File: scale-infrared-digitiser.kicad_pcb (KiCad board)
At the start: 2 copper layers, 8 x 166 mm, 115 parts, among them IC0 LM324PT, IC1 LM324PT, IC2 LM324PT, IC3 LM324PT, IC4 74HC4067PW,118, IC5 74HC4067PW,118, J0 Conn_02x04_TRNS, J1 Conn_02x04_RECV, Q1 T2N7002AK, Q10 T2N7002AK, Q11 T2N7002AK, Q12 T2N7002AK, Q13 T2N7002AK, Q14 T2N7002AK, Q15 T2N7002AK, Q16 T2N7002AK, Q2 T2N7002AK, Q3 T2N7002AK, Q4 T2N7002AK, Q5 T2N7002AK, Q6 T2N7002AK, Q7 T2N7002AK, Q8 T2N7002AK, Q9 T2N7002AK

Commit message: short sides almost complete
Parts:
- removed C13, C19, C25, C6: 1u, Capacitor_SMD:C_0603_1608Metric
- moved IC5 173.5 mm to (200.4, 96.5), turned to 90 degrees
- moved J1 173.4 mm to (206.9, 97.7), turned to 90 degrees
- moved LED0 140.6 mm to (70.1, 81.7), turned to 90 degrees
- moved D_photo15 139.0 mm to (190.9, 93.7), turned to 90 degrees
- moved LED1 138.3 mm to (78.2, 81.7), turned to 90 degrees
- moved Q1 136.9 mm to (69.7, 85.9), turned to 90 degrees
- moved LED2 136.0 mm to (86.2, 81.7), turned to 90 degrees
- moved LED3 133.7 mm to (94.3, 81.7), turned to 90 degrees
- moved D_photo14 129.0 mm to (182.9, 93.7), turned to 90 degrees
- moved Q2 128.3 mm to (81.4, 74.9), turned to 90 degrees
- moved R1 126.6 mm to (70.5, 70.6)
- moved D_photo11 125.5 mm to (158.7, 93.7), turned to 90 degrees
- moved Q3 125.1 mm to (86.0, 74.9), turned to 90 degrees
- moved Q4 122.2 mm to (90.7, 74.9), turned to 90 degrees
- moved D_photo13 119.5 mm to (174.8, 93.7), turned to 90 degrees
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- renumbered D_photo14 to D_photo10, D_photo15 to D_photo11, D_photo8 to D_photo12, D_photo9 to D_photo13, D_photo10 to D_photo14, D_photo11 to D_photo15, D_photo12 to D_photo8, D_photo13 to D_photo9
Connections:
- C21 pad 1: /PHT_DAT_8 -> /PHT_DAT_10
- C22 pad 2: /PHT_DAT_9 -> /PHT_DAT_11
- C23 pad 1: /PHT_DAT_10 -> /PHT_DAT_8
- C24 pad 2: /PHT_DAT_11 -> /PHT_DAT_9
- D_photo0 pad 1: /PHT_DAT_0 -> /PHT_DAT_1
- D_photo1 pad 1: /PHT_DAT_1 -> /PHT_DAT_0
- D_photo10 pad 1: /PHT_DAT_14 -> /PHT_DAT_15
- D_photo11 pad 1: /PHT_DAT_15 -> /PHT_DAT_14
- D_photo12 pad 1: /PHT_DAT_8 -> /PHT_DAT_11
- D_photo13 pad 1: /PHT_DAT_9 -> /PHT_DAT_10
- D_photo14 pad 1: /PHT_DAT_10 -> /PHT_DAT_9
- D_photo15 pad 1: /PHT_DAT_11 -> /PHT_DAT_8
- D_photo2 pad 1: /PHT_DAT_2 -> /PHT_DAT_3
- D_photo3 pad 1: /PHT_DAT_3 -> /PHT_DAT_2
- D_photo4 pad 1: /PHT_DAT_4 -> /PHT_DAT_5
- D_photo5 pad 1: /PHT_DAT_5 -> /PHT_DAT_4
- D_photo6 pad 1: /PHT_DAT_6 -> /PHT_DAT_7
- D_photo7 pad 1: /PHT_DAT_7 -> /PHT_DAT_6
- D_photo8 pad 1: /PHT_DAT_12 -> /PHT_DAT_13
- D_photo9 pad 1: /PHT_DAT_13 -> /PHT_DAT_12
- IC0 pad 4: /3V3 -> /3V3_RECV
- IC1 pad 4: /3V3 -> /3V3_RECV
- IC2 pad 4: /3V3 -> /3V3_RECV
- IC3 pad 13: /PHT_DAT_11 -> /PHT_DAT_9
- IC3 pad 2: /PHT_DAT_8 -> /PHT_DAT_10
- IC3 pad 4: /3V3 -> /3V3_RECV
- IC3 pad 6: /PHT_DAT_9 -> /PHT_DAT_11
- IC3 pad 9: /PHT_DAT_10 -> /PHT_DAT_8
- IC4 pad 12: GND -> GND1
- IC4 pad 15: GND -> GND1
- IC4 pad 24: /3V3 -> /3V3_TRNS
- IC5 pad 24: /3V3 -> /3V3_RECV
- J0 pad 5: /3V3 -> /3V3_TRNS
- J0 pad 7: GND -> GND1
- J0 pad 8: GND -> GND1
- J1 pad 1: /SEL_RECV_3 -> /MCU_RECV_DAT
- J1 pad 2: /SEL_RECV_2 -> /SEL_RECV_3
- J1 pad 3: /SEL_RECV_1 -> /SEL_RECV_0
- J1 pad 4: /SEL_RECV_0 -> /SEL_RECV_2
- J1 pad 5: /3V3 -> /SEL_RECV_1
- J1 pad 6: /MCU_RECV_DAT -> /3V3_RECV
- Q1 pad 2: GND -> GND1
- Q10 pad 2: GND -> GND1
- Q11 pad 2: GND -> GND1
- Q12 pad 2: GND -> GND1
- Q13 pad 2: GND -> GND1
- Q14 pad 2: GND -> GND1
- Q15 pad 2: GND -> GND1
- Q16 pad 2: GND -> GND1
- Q2 pad 2: GND -> GND1
- Q3 pad 2: GND -> GND1
- Q4 pad 2: GND -> GND1
- Q5 pad 2: GND -> GND1
- Q6 pad 2: GND -> GND1
- Q7 pad 2: GND -> GND1
- Q8 pad 2: GND -> GND1
- Q9 pad 2: GND -> GND1
- R1 pad 2: /3V3 -> /3V3_TRNS
- R10 pad 2: /3V3 -> /3V3_TRNS
- R11 pad 2: /3V3 -> /3V3_TRNS
- R12 pad 2: /3V3 -> /3V3_TRNS
- R13 pad 2: /3V3 -> /3V3_TRNS
- R14 pad 2: /3V3 -> /3V3_TRNS
- R15 pad 2: /3V3 -> /3V3_TRNS
- R16 pad 2: /3V3 -> /3V3_TRNS
- R18 pad 2: /3V3 -> /3V3_RECV
- R2 pad 2: /3V3 -> /3V3_TRNS
- R3 pad 2: /3V3 -> /3V3_TRNS
- R31 pad 2: /PHT_DAT_8 -> /PHT_DAT_10
- R32 pad 1: /PHT_DAT_9 -> /PHT_DAT_11
- R33 pad 2: /PHT_DAT_10 -> /PHT_DAT_8
- R34 pad 1: /PHT_DAT_11 -> /PHT_DAT_9
- R4 pad 2: /3V3 -> /3V3_TRNS
- R5 pad 2: /3V3 -> /3V3_TRNS
- R6 pad 2: /3V3 -> /3V3_TRNS
- R7 pad 2: /3V3 -> /3V3_TRNS
- R8 pad 2: /3V3 -> /3V3_TRNS
- R9 pad 2: /3V3 -> /3V3_TRNS
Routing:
- net /NON_INVERTING_REF: track 0.00 -> 261.5 mm, vias 0 -> 13
- net /3V3_RECV: track 0.00 -> 174.1 mm
- net /PHT_DAT_1: track 0.00 -> 141.5 mm, vias 0 -> 2
- net /PHT_DAT_0: track 0.00 -> 140.3 mm, vias 0 -> 2
- net /PHT_DAT_3: track 0.00 -> 130.5 mm, vias 0 -> 2
- net /PHT_DAT_2: track 0.00 -> 128.4 mm
- net /PHT_DAT_5: track 0.00 -> 103.9 mm, vias 0 -> 2
- net /PHT_DAT_4: track 0.00 -> 101.3 mm, vias 0 -> 2
- net /PHT_DAT_6: track 0.00 -> 93.3 mm, vias 0 -> 3
- net /PHT_DAT_7: track 0.00 -> 91.5 mm, vias 0 -> 2
- net /PHT_DAT_13: track 0.00 -> 76.6 mm, vias 0 -> 2
- net /PHT_DAT_12: track 0.00 -> 70.0 mm, vias 0 -> 2
- net /PHT_DAT_14: track 0.00 -> 62.0 mm, vias 0 -> 2
- net /PHT_DAT_15: track 0.00 -> 61.5 mm, vias 0 -> 2
- net /PHT_DAT_11: track 0.00 -> 44.6 mm
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- added copper zone on B.Cu, net GND
- added copper zone on B.Cu, net GND1
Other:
- board size 8 x 166 mm -> 150.5 x 24 mm
- board text added: "Screen outline dimension: 127.6mm x 173.8mm"

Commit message: laptop work
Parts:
- moved R16 30.7 mm to (193.0, 84.5), turned to 0 degrees
- moved R1 14.0 mm to (72.2, 84.5)
- moved Q5 12.6 mm to (92.4, 86.5)
- moved Q6 12.6 mm to (97.0, 86.5)
- moved Q7 12.6 mm to (101.6, 86.5)
- moved Q8 12.6 mm to (106.2, 86.5)
- moved Q2 12.3 mm to (77.5, 86.5)
- moved Q3 12.3 mm to (82.1, 86.5)
- moved Q4 12.3 mm to (86.7, 86.5)
- moved Q12 12.2 mm to (126.0, 86.5)
- moved Q10 12.2 mm to (116.7, 86.5)
- moved Q11 12.2 mm to (121.3, 86.5)
- moved Q13 12.2 mm to (131.8, 86.5)
- moved Q14 12.2 mm to (136.4, 86.5)
- moved Q15 12.2 mm to (141.0, 86.5)
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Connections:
- C21 pad 1: /PHT_DAT_10 -> /PHT_DAT_11
- C22 pad 2: /PHT_DAT_11 -> /PHT_DAT_10
- C23 pad 1: /PHT_DAT_8 -> /PHT_DAT_9
- C24 pad 2: /PHT_DAT_9 -> /PHT_DAT_8
- D_photo12 pad 1: /PHT_DAT_11 -> /PHT_DAT_10
- D_photo13 pad 1: /PHT_DAT_10 -> /PHT_DAT_11
- D_photo14 pad 1: /PHT_DAT_9 -> /PHT_DAT_8
- D_photo15 pad 1: /PHT_DAT_8 -> /PHT_DAT_9
- IC3 pad 13: /PHT_DAT_9 -> /PHT_DAT_8
- IC3 pad 2: /PHT_DAT_10 -> /PHT_DAT_11
- IC3 pad 6: /PHT_DAT_11 -> /PHT_DAT_10
- IC3 pad 9: /PHT_DAT_8 -> /PHT_DAT_9
- IC4 pad 1: /MCU_TRNS_CTL -> /LED_CTL_7
- IC4 pad 10: /SEL_TRNS_0 -> /SEL_TRNS_3
- IC4 pad 13: /SEL_TRNS_3 -> /SEL_TRNS_0
- IC4 pad 2: /LED_CTL_7 -> /LED_CTL_6
- IC4 pad 3: /LED_CTL_6 -> /LED_CTL_5
- IC4 pad 4: /LED_CTL_5 -> /LED_CTL_4
- IC4 pad 5: /LED_CTL_4 -> /LED_CTL_3
- IC4 pad 6: /LED_CTL_3 -> /LED_CTL_2
- IC4 pad 7: /LED_CTL_2 -> /LED_CTL_1
- IC4 pad 8: /LED_CTL_1 -> /LED_CTL_0
- IC4 pad 9: /LED_CTL_0 -> /MCU_TRNS_CTL
- J0 pad 5: /3V3_TRNS -> /MCU_TRNS_CTL
- J0 pad 6: /MCU_TRNS_CTL -> /3V3_TRNS
- R31 pad 2: /PHT_DAT_10 -> /PHT_DAT_11
- R32 pad 1: /PHT_DAT_11 -> /PHT_DAT_10
- R33 pad 2: /PHT_DAT_8 -> /PHT_DAT_9
- R34 pad 1: /PHT_DAT_9 -> /PHT_DAT_8
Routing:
- net /3V3_TRNS: track 0.00 -> 147.6 mm
- net /MCU_TRNS_CTL: track 0.00 -> 13.5 mm
- net /SEL_TRNS_1: track 0.00 -> 9.53 mm
- net /SEL_TRNS_0: track 0.00 -> 6.44 mm
- net /SEL_TRNS_3: track 0.00 -> 6.02 mm
- net /SEL_TRNS_2: track 0.00 -> 5.10 mm
- net Net-(LED0-K): track 0.00 -> 4.43 mm
- net Net-(LED15-A): track 0.00 -> 3.11 mm
- net Net-(LED0-A): track 0.00 -> 3.05 mm
- net GND1: vias 2 -> 3

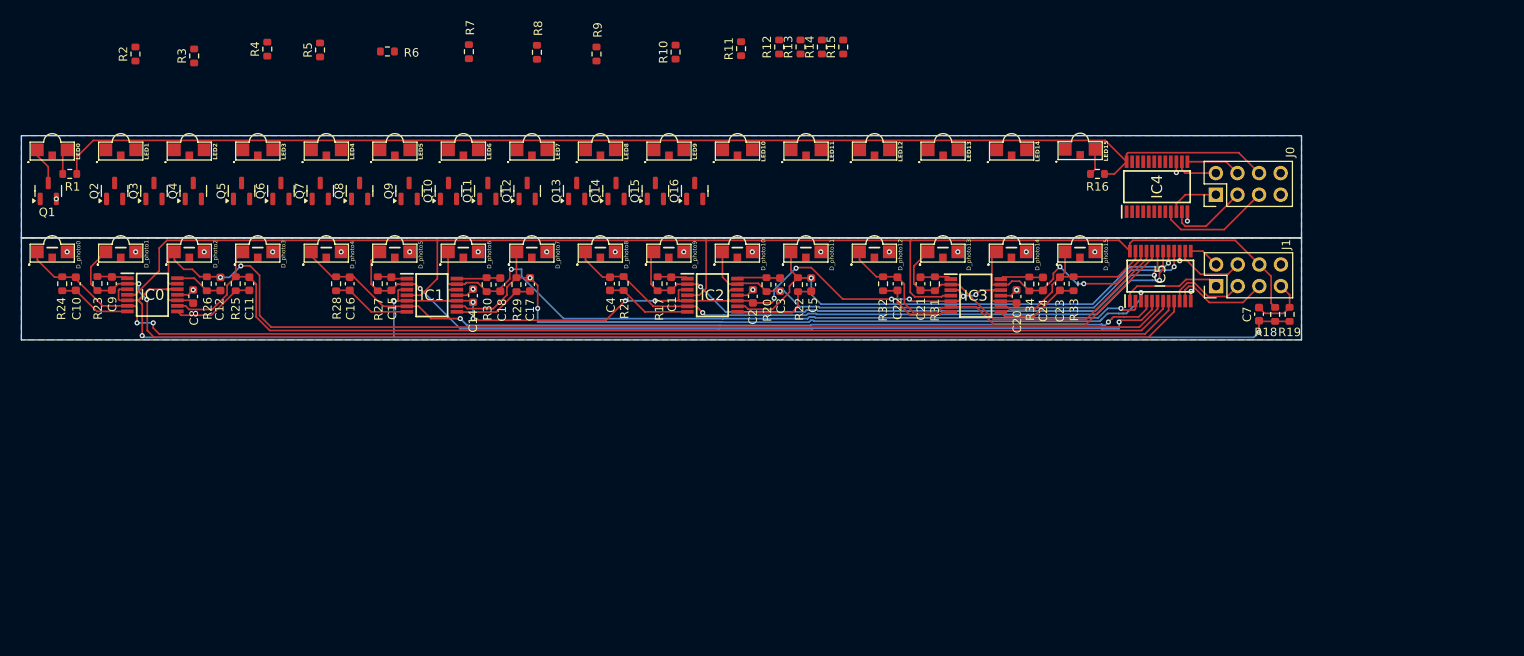
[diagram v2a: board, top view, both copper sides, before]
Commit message: reworking PCB for new dimensions
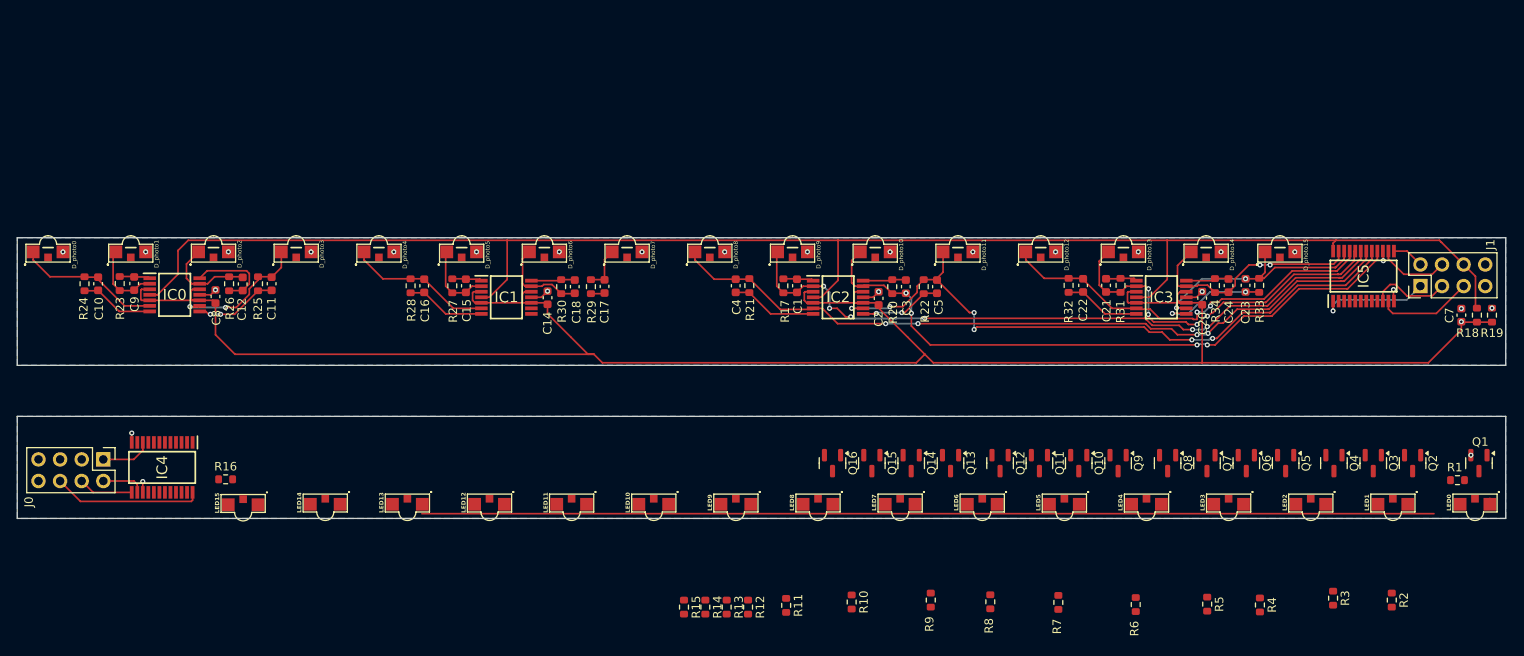
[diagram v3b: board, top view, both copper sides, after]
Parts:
- moved LED0 172.4 mm to (237.4, 123.3), turned to -90 degrees
- moved Q1 171.2 mm to (237.8, 118.5), turned to -90 degrees
- moved R1 167.1 mm to (235.3, 120.5), turned to 180 degrees
- moved R2 161.0 mm to (227.6, 134.6), turned to -90 degrees
- moved Q2 155.9 mm to (230.1, 118.5), turned to -90 degrees
- moved LED1 155.3 mm to (227.7, 123.3), turned to -90 degrees
- moved R3 148.3 mm to (220.7, 134.4), turned to -90 degrees
- moved Q3 146.9 mm to (225.4, 118.5), turned to -90 degrees
- moved LED2 138.3 mm to (218.1, 123.3), turned to -90 degrees
- moved Q4 137.9 mm to (220.8, 118.5), turned to -90 degrees
- moved J0 134.5 mm to (76.1, 118.1), turned to -90 degrees
- moved R4 133.8 mm to (212.1, 135.2), turned to -90 degrees
- moved Q5 126.9 mm to (215.1, 118.5), turned to -90 degrees
- moved R5 123.0 mm to (205.9, 135.1), turned to -90 degrees
- moved IC4 121.5 mm to (83.0, 119.0), turned to -90 degrees
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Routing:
- net /PHT_DAT_0: track 140.3 -> 8.86 mm, vias 2 -> 0
- net /PHT_DAT_1: track 141.5 -> 17.0 mm, vias 2 -> 0
- net /PHT_DAT_3: track 130.5 -> 11.0 mm, vias 2 -> 0
- net /PHT_DAT_2: track 128.4 -> 16.4 mm, vias 0 -> 2
- net /PHT_DAT_4: track 101.3 -> 8.93 mm, vias 2 -> 0
- net /PHT_DAT_6: track 93.3 -> 5.27 mm, vias 3 -> 0
- net /PHT_DAT_5: track 103.9 -> 17.1 mm, vias 2 -> 0
- net /PHT_DAT_7: track 91.5 -> 10.9 mm, vias 2 -> 0
- net /NON_INVERTING_REF: track 261.5 -> 237.0 mm, vias 13 -> 1
- net /3V3_RECV: track 174.1 -> 193.2 mm
- net /PHT_DAT_14: track 62.0 -> 77.1 mm, vias 2 -> 6
- net /PHT_DAT_15: track 61.5 -> 76.1 mm, vias 2 -> 4
- net /MCU_TRNS_CTL: track 13.5 -> 0.00 mm
- net /PHT_DAT_13: track 76.6 -> 88.4 mm, vias 2 -> 4
- net /3V3_TRNS: track 147.6 -> 136.1 mm
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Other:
- board size 150.5 x 24 mm -> 175 x 33 mm
- board text added: "Screen outline dimension: 160mm x 160mm"
- board text removed: "Screen outline dimension: 127.6mm x 173.8mm"

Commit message: completed design ready for review before assembly
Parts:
- added REF**: mouse_bites, manufacturing:mouse_bites, F.Cu at (75.0, 110.0)
- added REF**: mouse_bites, manufacturing:mouse_bites, F.Cu at (135.0, 110.0)
- added REF**: mouse_bites, manufacturing:mouse_bites, F.Cu at (221.0, 110.0)
- added REF**: mouse_bites, manufacturing:mouse_bites, F.Cu at (177.0, 110.0)
- added REF**: mouse_bites, manufacturing:mouse_bites, F.Cu at (199.0, 110.0)
- added REF**: mouse_bites, manufacturing:mouse_bites, F.Cu at (139.0, 110.0)
- added REF**: mouse_bites, manufacturing:mouse_bites, F.Cu at (125.0, 110.0)
- added REF**: mouse_bites, manufacturing:mouse_bites, F.Cu at (69.0, 110.0)
- added REF**: mouse_bites, manufacturing:mouse_bites, F.Cu at (99.0, 110.0)
- added REF**: mouse_bites, manufacturing:mouse_bites, F.Cu at (203.0, 110.0)
- added REF**: mouse_bites, manufacturing:mouse_bites, F.Cu at (77.0, 110.0)
- added REF**: mouse_bites, manufacturing:mouse_bites, F.Cu at (87.0, 110.0)
- added REF**: mouse_bites, manufacturing:mouse_bites, F.Cu at (127.0, 110.0)
- added REF**: mouse_bites, manufacturing:mouse_bites, F.Cu at (73.0, 110.0)
- added REF**: mouse_bites, manufacturing:mouse_bites, F.Cu at (217.0, 110.0)
- added REF**: mouse_bites, manufacturing:mouse_bites, F.Cu at (129.0, 110.0)
- added REF**: mouse_bites, manufacturing:mouse_bites, F.Cu at (179.0, 110.0)
- added REF**: mouse_bites, manufacturing:mouse_bites, F.Cu at (231.0, 110.0)
- added REF**: mouse_bites, manufacturing:mouse_bites, F.Cu at (187.0, 110.0)
- added REF**: mouse_bites, manufacturing:mouse_bites, F.Cu at (195.0, 110.0)
- added REF**: mouse_bites, manufacturing:mouse_bites, F.Cu at (149.0, 110.0)
- added REF**: mouse_bites, manufacturing:mouse_bites, F.Cu at (157.0, 110.0)
- added REF**: mouse_bites, manufacturing:mouse_bites, F.Cu at (173.0, 110.0)
- added REF**: mouse_bites, manufacturing:mouse_bites, F.Cu at (167.0, 110.0)
- added REF**: mouse_bites, manufacturing:mouse_bites, F.Cu at (107.0, 110.0)
- added REF**: mouse_bites, manufacturing:mouse_bites, F.Cu at (141.0, 110.0)
- added REF**: mouse_bites, manufacturing:mouse_bites, F.Cu at (121.0, 110.0)
- added REF**: mouse_bites, manufacturing:mouse_bites, F.Cu at (213.0, 110.0)
- added REF**: mouse_bites, manufacturing:mouse_bites, F.Cu at (153.0, 110.0)
- added REF**: mouse_bites, manufacturing:mouse_bites, F.Cu at (193.0, 110.0)
- added REF**: mouse_bites, manufacturing:mouse_bites, F.Cu at (105.0, 110.0)
- added REF**: mouse_bites, manufacturing:mouse_bites, F.Cu at (119.0, 110.0)
- added REF**: mouse_bites, manufacturing:mouse_bites, F.Cu at (147.0, 110.0)
- added REF**: mouse_bites, manufacturing:mouse_bites, F.Cu at (233.0, 110.0)
- added REF**: mouse_bites, manufacturing:mouse_bites, F.Cu at (131.0, 110.0)
- added REF**: mouse_bites, manufacturing:mouse_bites, F.Cu at (201.0, 110.0)
- added REF**: mouse_bites, manufacturing:mouse_bites, F.Cu at (97.0, 110.0)
- added REF**: mouse_bites, manufacturing:mouse_bites, F.Cu at (71.0, 110.0)
- added REF**: mouse_bites, manufacturing:mouse_bites, F.Cu at (91.0, 110.0)
- added REF**: mouse_bites, manufacturing:mouse_bites, F.Cu at (185.0, 110.0)
- added REF**: mouse_bites, manufacturing:mouse_bites, F.Cu at (225.0, 110.0)
- added REF**: mouse_bites, manufacturing:mouse_bites, F.Cu at (175.0, 110.0)
- added REF**: mouse_bites, manufacturing:mouse_bites, F.Cu at (215.0, 110.0)
- added REF**: mouse_bites, manufacturing:mouse_bites, F.Cu at (197.0, 110.0)
- added REF**: mouse_bites, manufacturing:mouse_bites, F.Cu at (205.0, 110.0)
- added REF**: mouse_bites, manufacturing:mouse_bites, F.Cu at (83.0, 110.0)
- added REF**: mouse_bites, manufacturing:mouse_bites, F.Cu at (191.0, 110.0)
- added REF**: mouse_bites, manufacturing:mouse_bites, F.Cu at (101.0, 110.0)
- added REF**: mouse_bites, manufacturing:mouse_bites, F.Cu at (235.0, 110.0)
- added REF**: mouse_bites, manufacturing:mouse_bites, F.Cu at (123.0, 110.0)
- added REF**: mouse_bites, manufacturing:mouse_bites, F.Cu at (171.0, 110.0)
- added REF**: mouse_bites, manufacturing:mouse_bites, F.Cu at (223.0, 110.0)
- added REF**: mouse_bites, manufacturing:mouse_bites, F.Cu at (211.0, 110.0)
- added REF**: mouse_bites, manufacturing:mouse_bites, F.Cu at (237.0, 110.0)
- added REF**: mouse_bites, manufacturing:mouse_bites, F.Cu at (113.0, 110.0)
- added REF**: mouse_bites, manufacturing:mouse_bites, F.Cu at (161.0, 110.0)
- added REF**: mouse_bites, manufacturing:mouse_bites, F.Cu at (151.0, 110.0)
- added REF**: mouse_bites, manufacturing:mouse_bites, F.Cu at (93.0, 110.0)
- added REF**: mouse_bites, manufacturing:mouse_bites, F.Cu at (89.0, 110.0)
- added REF**: mouse_bites, manufacturing:mouse_bites, F.Cu at (79.0, 110.0)
- added REF**: mouse_bites, manufacturing:mouse_bites, F.Cu at (169.0, 110.0)
- added REF**: mouse_bites, manufacturing:mouse_bites, F.Cu at (229.0, 110.0)
- added REF**: mouse_bites, manufacturing:mouse_bites, F.Cu at (145.0, 110.0)
- added REF**: mouse_bites, manufacturing:mouse_bites, F.Cu at (183.0, 110.0)
- added REF**: mouse_bites, manufacturing:mouse_bites, F.Cu at (209.0, 110.0)
- added REF**: mouse_bites, manufacturing:mouse_bites, F.Cu at (189.0, 110.0)
- added REF**: mouse_bites, manufacturing:mouse_bites, F.Cu at (165.0, 110.0)
- added REF**: mouse_bites, manufacturing:mouse_bites, F.Cu at (115.0, 110.0)
- added REF**: mouse_bites, manufacturing:mouse_bites, F.Cu at (227.0, 110.0)
- added REF**: mouse_bites, manufacturing:mouse_bites, F.Cu at (155.0, 110.0)
- added REF**: mouse_bites, manufacturing:mouse_bites, F.Cu at (81.0, 110.0)
- added REF**: mouse_bites, manufacturing:mouse_bites, F.Cu at (159.0, 110.0)
- added REF**: mouse_bites, manufacturing:mouse_bites, F.Cu at (239.0, 110.0)
- added REF**: mouse_bites, manufacturing:mouse_bites, F.Cu at (137.0, 110.0)
- added REF**: mouse_bites, manufacturing:mouse_bites, F.Cu at (109.0, 110.0)
- added REF**: mouse_bites, manufacturing:mouse_bites, F.Cu at (181.0, 110.0)
- added REF**: mouse_bites, manufacturing:mouse_bites, F.Cu at (85.0, 110.0)
- added REF**: mouse_bites, manufacturing:mouse_bites, F.Cu at (111.0, 110.0)
- added REF**: mouse_bites, manufacturing:mouse_bites, F.Cu at (133.0, 110.0)
- added REF**: mouse_bites, manufacturing:mouse_bites, F.Cu at (207.0, 110.0)
- added REF**: mouse_bites, manufacturing:mouse_bites, F.Cu at (117.0, 110.0)
- added REF**: mouse_bites, manufacturing:mouse_bites, F.Cu at (103.0, 110.0)
- added REF**: mouse_bites, manufacturing:mouse_bites, F.Cu at (67.0, 110.0)
- added REF**: mouse_bites, manufacturing:mouse_bites, F.Cu at (163.0, 110.0)
- added REF**: mouse_bites, manufacturing:mouse_bites, F.Cu at (143.0, 110.0)
- added REF**: mouse_bites, manufacturing:mouse_bites, F.Cu at (219.0, 110.0)
- added REF**: mouse_bites, manufacturing:mouse_bites, F.Cu at (95.0, 110.0)
- moved Q16 71.3 mm to (90.5, 118.5)
- moved Q15 66.3 mm to (100.2, 118.5)
- moved Q14 61.3 mm to (109.8, 118.5)
- moved Q13 56.2 mm to (119.5, 118.5)
- moved Q12 52.4 mm to (129.1, 118.5)
- moved Q11 47.4 mm to (138.8, 118.5)
- moved R15 43.0 mm to (104.2, 120.4), turned to 180 degrees
- moved Q10 42.3 mm to (148.5, 118.5)
- moved Q9 37.3 mm to (158.1, 118.5)
- moved R14 36.4 mm to (113.8, 120.4), turned to 180 degrees
- moved Q8 33.5 mm to (167.8, 118.5)
- moved R13 30.0 mm to (123.4, 120.4), turned to 180 degrees
- moved Q7 28.4 mm to (177.4, 118.5)
- moved R12 24.1 mm to (133.1, 120.4), turned to 180 degrees
- moved Q6 23.4 mm to (187.1, 118.5)
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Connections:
- IC4 pad 1: /LED_CTL_7 -> /LED_CTL_5
- IC4 pad 16: /LED_CTL_15 -> /LED_CTL_8
- IC4 pad 17: /LED_CTL_14 -> /LED_CTL_9
- IC4 pad 18: /LED_CTL_13 -> /LED_CTL_10
- IC4 pad 19: /LED_CTL_12 -> /LED_CTL_11
- IC4 pad 20: /LED_CTL_11 -> /LED_CTL_12
- IC4 pad 21: /LED_CTL_10 -> /LED_CTL_13
- IC4 pad 22: /LED_CTL_9 -> /LED_CTL_14
- IC4 pad 23: /LED_CTL_8 -> /LED_CTL_15
- IC4 pad 3: /LED_CTL_5 -> /LED_CTL_7
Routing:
- net /LED_CTL_0: track 0.00 -> 159.1 mm
- net /PHT_DAT_0: track 8.86 -> 167.0 mm, vias 0 -> 2
- net /LED_CTL_1: track 0.00 -> 148.1 mm
- net /PHT_DAT_1: track 17.0 -> 163.6 mm, vias 0 -> 6
- net /PHT_DAT_3: track 11.0 -> 152.6 mm, vias 0 -> 8
- net /PHT_DAT_2: track 16.4 -> 155.7 mm, vias 2 -> 8
- net /LED_CTL_2: track 0.00 -> 137.5 mm
- net /3V3_TRNS: track 136.1 -> 1.76 mm, vias 0 -> 17
- net /LED_CTL_3: track 0.00 -> 126.8 mm
- net /LED_CTL_4: track 0.00 -> 116.0 mm
- net /PHT_DAT_4: track 8.93 -> 119.6 mm, vias 0 -> 6
- net /PHT_DAT_6: track 5.27 -> 111.1 mm, vias 0 -> 6
- net /PHT_DAT_5: track 17.1 -> 121.6 mm, vias 0 -> 6
- net /LED_CTL_5: track 0.00 -> 103.5 mm
- net /PHT_DAT_7: track 10.9 -> 109.6 mm, vias 0 -> 6
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- added copper zone on B.Cu, net /3V3_TRNS
- added copper zone on F.Cu, net GND
- added copper zone on F.Cu, net GND1
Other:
- outline, holes or cut-outs redrawn
